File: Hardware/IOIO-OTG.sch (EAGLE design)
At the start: 53 parts, among them Q1 IRLML2244, Q2 2N7002PW, U1 PIC24FJ256GB206, U14 SWITCH_SPDT, U2 TPS6214X"", U3 VREG_MIC5216

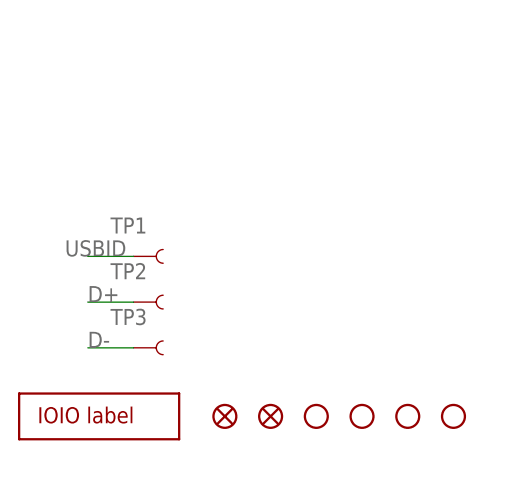
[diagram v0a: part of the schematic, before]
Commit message: More changes:
-removed test-points from below the microAB
-Moved "PWR" LED and RES out just a bit more to clear headers on the OTG
w/ Headers
-Created and added a new TRIMPOT FP per Bob's request
-Added T-Stop around the PIC to allow Tyler T. to be able to inspect the
PIC with the AOI
-Also added a new new microAB FP
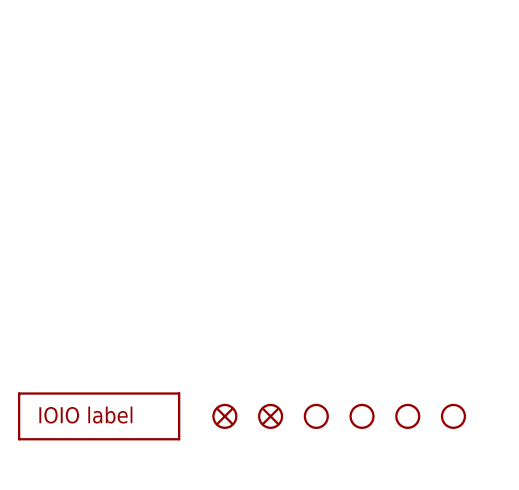
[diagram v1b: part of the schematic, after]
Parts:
- removed TP1, TP2, TP3: TEST-POINT3, SparkFun-Passives:TEST-POINT3
- R3: device SparkFun-Electromechanical:TRIMPOTTRIMPOT-5MM -> Testing:TRIMPOTSMD_STANDARD
- U4: device Testing:USB-AB"" -> Testing:USB-AB"""
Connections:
- net D+: no longer TP2.1
- net D-: no longer TP3.1
- net USBID: no longer TP1.1
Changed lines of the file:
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@@
 <part name="JP1" library="SparkFun" deviceset="M03" device="PTH" value="VIN"/>
 <part name="JP3" library="SparkFun" deviceset="M01" device="PTH"/>
-<part name="R3" library="SparkFun-Electromechanical" deviceset="TRIMPOT" device="TRIMPOT-5MM" value="TS53YL502MR10">
+<part name="R3" library="Testing" deviceset="TRIMPOT" device="SMD_STANDARD" value="TS53YL502MR10">
 <attribute name="PART#" value="TS53YL502MR10"/>
 </part>
@@
 <part name="JP8" library="SparkFun" deviceset="FIDUCIAL" device="UFIDUCIAL"/>
 <part name="JP16" library="SparkFun" deviceset="FIDUCIAL" device="UFIDUCIAL"/>
-<part name="TP1" library="SparkFun-Passives" deviceset="TEST-POINT" device="3"/>
-<part name="TP2" library="SparkFun-Passives" deviceset="TEST-POINT" device="3"/>
-<part name="TP3" library="SparkFun-Passives" deviceset="TEST-POINT" device="3"/>
 <part name="U$6" library="SparkFun-Aesthetics" deviceset="IOIO-OTG" device=""/>
-<part name="U4" library="Testing" deviceset="USB-AB" device="&quot;&quot;"/>
+<part name="U4" library="Testing" deviceset="USB-AB" device="&quot;&quot;&quot;"/>
 <part name="U2" library="SparkFun-PowerIC" deviceset="TPS6214X" device="&quot;&quot;"/>
 </parts>
@@
 <instance part="JP8" gate="G$1" x="27.94" y="10.16"/>
 <instance part="JP16" gate="G$1" x="33.02" y="10.16"/>
-<instance part="TP1" gate="G$1" x="17.78" y="27.94" smashed="yes">
-<attribute name="NAME" x="15.24" y="30.48" size="1.778" layer="95"/>
-</instance>
-<instance part="TP2" gate="G$1" x="17.78" y="22.86" smashed="yes">
-<attribute name="NAME" x="15.24" y="25.4" size="1.778" layer="95"/>
-</instance>
-<instance part="TP3" gate="G$1" x="17.78" y="17.78" smashed="yes">
-<attribute name="NAME" x="15.24" y="20.32" size="1.778" layer="95"/>
-</instance>
 <instance part="U$6" gate="G$1" x="5.08" y="7.62"/>
 <instance part="U4" gate="G$1" x="254" y="53.34" rot="MR180"/>
@@
 <pinref part="U4" gate="G$1" pin="D-"/>
 </segment>
-<segment>
-<pinref part="TP3" gate="G$1" pin="1"/>
-<wire x1="17.78" y1="17.78" x2="12.7" y2="17.78" width="0.1524" layer="91"/>
-<label x="12.7" y="17.78" size="1.778" layer="95"/>
-</segment>
 </net>
 <net name="D+" class="0">
@@
 <label x="203.2" y="53.34" size="1.778" layer="95"/>
 <pinref part="U4" gate="G$1" pin="D+"/>
-</segment>
-<segment>
-<pinref part="TP2" gate="G$1" pin="1"/>
-<wire x1="17.78" y1="22.86" x2="12.7" y2="22.86" width="0.1524" layer="91"/>
-<label x="12.7" y="22.86" size="1.778" layer="95"/>
 </segment>
 </net>
@@
 <label x="68.58" y="66.04" size="1.778" layer="95"/>
 </segment>
-<segment>
-<pinref part="TP1" gate="G$1" pin="1"/>
-<wire x1="17.78" y1="27.94" x2="12.7" y2="27.94" width="0.1524" layer="91"/>
-<label x="10.16" y="27.94" size="1.778" layer="95"/>
-</segment>
-</net>
+</net>

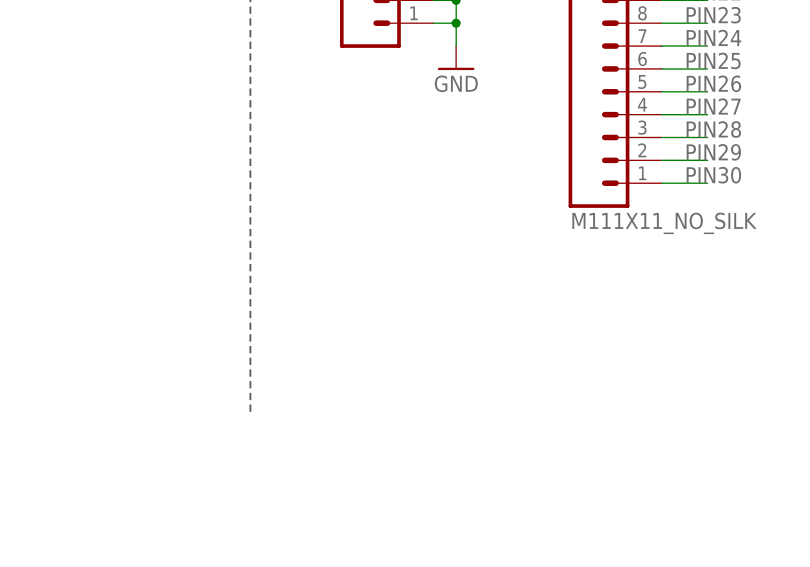
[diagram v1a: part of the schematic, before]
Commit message: Added VBUS test-point and Tstop around VREG
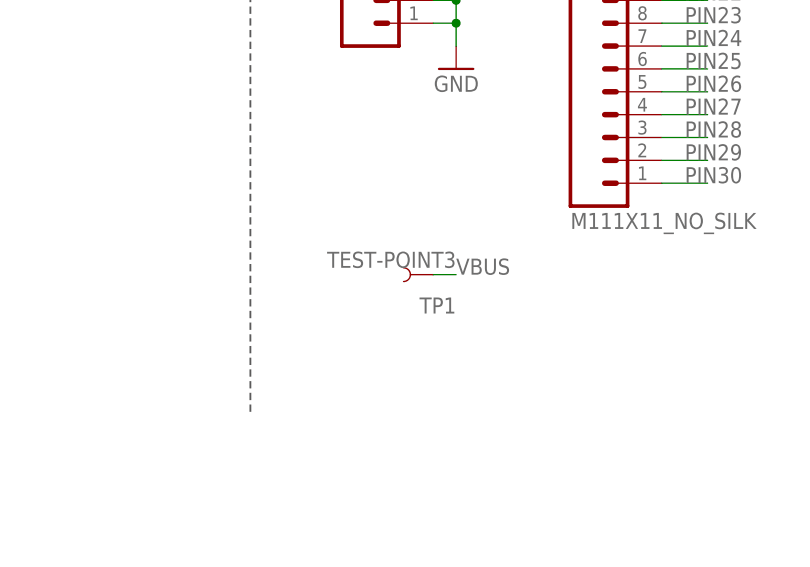
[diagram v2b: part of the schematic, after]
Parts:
- added TP1: TEST-POINT3, SparkFun-Passives:TEST-POINT3
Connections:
- net VBUS: now also TP1.1
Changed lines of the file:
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@@
 <part name="U4" library="Testing" deviceset="USB-AB" device="&quot;&quot;&quot;"/>
 <part name="U2" library="SparkFun-PowerIC" deviceset="TPS6214X" device="&quot;&quot;"/>
+<part name="TP1" library="SparkFun-Passives" deviceset="TEST-POINT" device="3"/>
 </parts>
 <sheets>
@@
 <instance part="U4" gate="G$1" x="254" y="53.34" rot="MR180"/>
 <instance part="U2" gate="G$1" x="111.76" y="228.6"/>
+<instance part="TP1" gate="G$1" x="309.88" y="38.1" rot="R180"/>
 </instances>
 <busses>
@@
 <label x="281.94" y="226.06" size="1.778" layer="95"/>
 </segment>
-</net>
+<segment>
+<pinref part="TP1" gate="G$1" pin="1"/>
+<wire x1="309.88" y1="38.1" x2="312.42" y2="38.1" width="0.1524" layer="91"/>
+<label x="312.42" y="38.1" size="1.778" layer="95"/>
+</segment>
+</net>

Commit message: Consistency fixes
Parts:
- C10: device SparkFun-Passives:CAP_POL1206 -> SparkFun-Capacitors:CAP_POL1206
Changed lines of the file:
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@@
 </part>
 <part name="R2" library="SparkFun-Resistors" deviceset="RESISTOR" device="0603-RES" value="100k"/>
-<part name="C10" library="SparkFun-Passives" deviceset="CAP_POL" device="1206" value="10uF">
+<part name="C10" library="SparkFun-Capacitors" deviceset="CAP_POL" device="1206" value="10uF">
 <attribute name="PART#" value="TAJA106K016RNJ"/>
 </part>

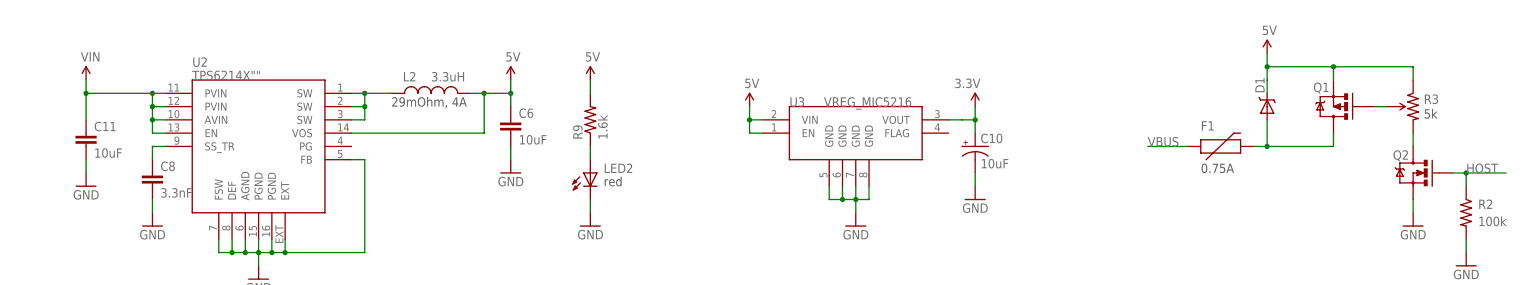
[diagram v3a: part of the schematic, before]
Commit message: Final 6.5.0 inconsistency fixes
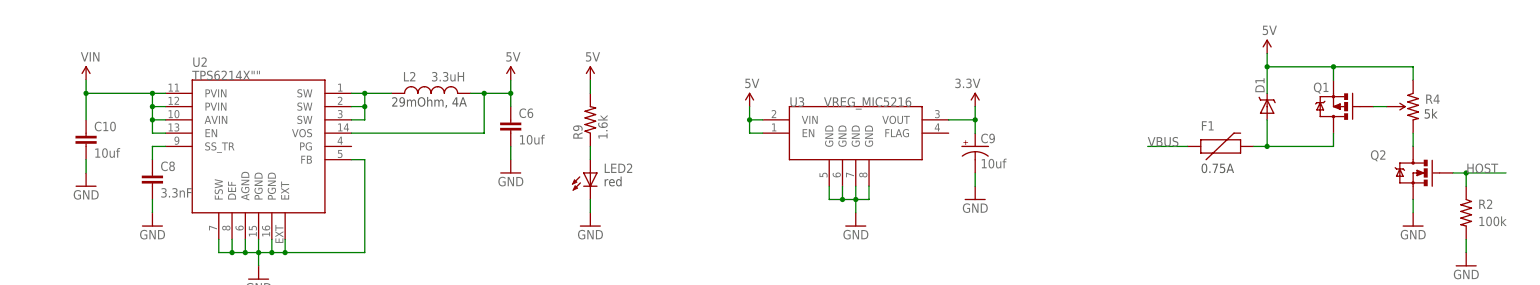
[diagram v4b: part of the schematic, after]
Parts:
- removed C11: 10uF, SparkFun-Passives:CAP1210
- added C9: 10uf, SparkFun-Capacitors:CAP_POL1206
- C10: value 10uF -> 10uf; device SparkFun-Capacitors:CAP_POL1206 -> SparkFun-Passives:CAP1210; PART# TAJA106K016RNJ -> (none)
- C6: value 10uF -> 10uf; PART# LMK212BJ106KG-T -> (none)
- D1: value B340A -> DIODE-SCHOTTKY_; PART# B340A -> (none)
- F1: PART# 0ZCA0075FF2G -> (none)
- Q2: value 2N7002PW -> MOSFET-NCHANNEL2N7002PW"; device SparkFun-DiscreteSemi:MOSFET-NCHANNELSOT323 -> SparkFun-DiscreteSemi:MOSFET-NCHANNEL2N7002PW"; PART# 2N7002PW -> (none)
- R4: value TS53YL502MR10 -> TRIMPOTSMD_STANDARD; PART# TS53YL502MR10 -> (none)
- renumbered R3 to R4
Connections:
- net 3.3V: now also C9.+; no longer C10.+
- net GND: now also C10.2, C9.-; no longer C10.-, C11.2
- net VIN: now also C10.1; no longer C11.1

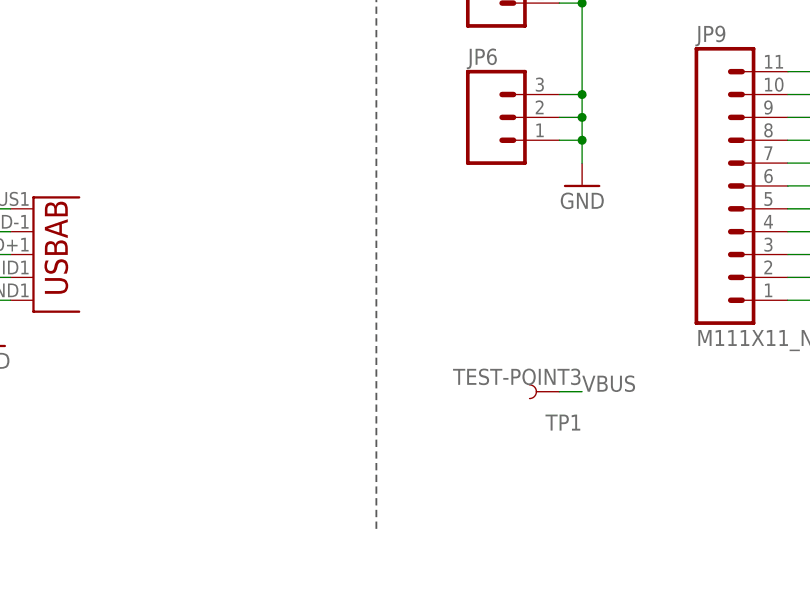
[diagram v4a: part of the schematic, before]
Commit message: Added test-points
3 new test-points:
D+
D-
USBID
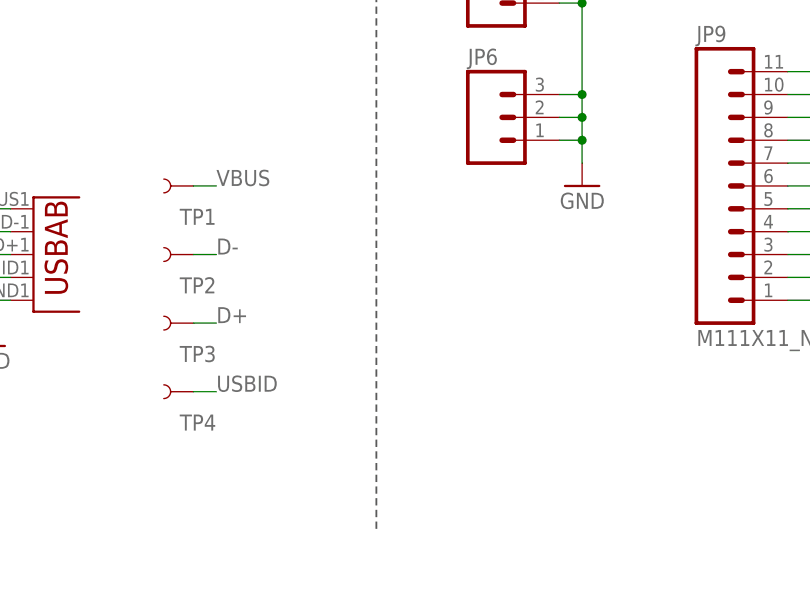
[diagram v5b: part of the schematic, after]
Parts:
- added TP2, TP3, TP4: TEST-POINT3, SparkFun-Passives:TEST-POINT3
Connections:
- net D+: now also TP3.1
- net D-: now also TP2.1
- net USBID: now also TP4.1
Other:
- moved on the sheet: TP1
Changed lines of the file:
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@@
 <part name="Q2" library="SparkFun-DiscreteSemi" deviceset="MOSFET-NCHANNEL" device="2N7002PW&quot;"/>
 <part name="R4" library="Testing" deviceset="TRIMPOT" device="SMD_STANDARD"/>
+<part name="TP2" library="SparkFun-Passives" deviceset="TEST-POINT" device="3"/>
+<part name="TP3" library="SparkFun-Passives" deviceset="TEST-POINT" device="3"/>
+<part name="TP4" library="SparkFun-Passives" deviceset="TEST-POINT" device="3"/>
 </parts>
 <sheets>
@@
 <instance part="U4" gate="G$1" x="254" y="53.34" rot="MR180"/>
 <instance part="U2" gate="G$1" x="111.76" y="228.6"/>
-<instance part="TP1" gate="G$1" x="309.88" y="38.1" rot="R180"/>
+<instance part="TP1" gate="G$1" x="269.24" y="60.96" smashed="yes" rot="R180">
+<attribute name="NAME" x="271.78" y="58.42" size="1.778" layer="95" rot="R180"/>
+</instance>
 <instance part="C9" gate="G$1" x="248.92" y="226.06"/>
 <instance part="C10" gate="G$1" x="78.74" y="226.06"/>
@@
 <instance part="R4" gate="R?" x="332.74" y="233.68" smashed="yes" rot="MR270">
 <attribute name="NAME" x="335.026" y="235.9914" size="1.778" layer="95" rot="MR180"/>
+</instance>
+<instance part="TP2" gate="G$1" x="269.24" y="53.34" smashed="yes" rot="R180">
+<attribute name="NAME" x="271.78" y="50.8" size="1.778" layer="95" rot="R180"/>
+</instance>
+<instance part="TP3" gate="G$1" x="269.24" y="45.72" smashed="yes" rot="R180">
+<attribute name="NAME" x="271.78" y="43.18" size="1.778" layer="95" rot="R180"/>
+</instance>
+<instance part="TP4" gate="G$1" x="269.24" y="38.1" smashed="yes" rot="R180">
+<attribute name="NAME" x="271.78" y="35.56" size="1.778" layer="95" rot="R180"/>
 </instance>
 </instances>
@@
 <pinref part="U4" gate="G$1" pin="D-"/>
 </segment>
+<segment>
+<pinref part="TP2" gate="G$1" pin="1"/>
+<wire x1="269.24" y1="53.34" x2="271.78" y2="53.34" width="0.1524" layer="91"/>
+<label x="271.78" y="53.34" size="1.778" layer="95"/>
+</segment>
 </net>
 <net name="D+" class="0">
@@
 <label x="203.2" y="53.34" size="1.778" layer="95"/>
 <pinref part="U4" gate="G$1" pin="D+"/>
+</segment>
+<segment>
+<pinref part="TP3" gate="G$1" pin="1"/>
+<wire x1="269.24" y1="45.72" x2="271.78" y2="45.72" width="0.1524" layer="91"/>
+<label x="271.78" y="45.72" size="1.778" layer="95"/>
 </segment>
 </net>
@@
 <label x="68.58" y="66.04" size="1.778" layer="95"/>
 </segment>
+<segment>
+<pinref part="TP4" gate="G$1" pin="1"/>
+<wire x1="269.24" y1="38.1" x2="271.78" y2="38.1" width="0.1524" layer="91"/>
+<label x="271.78" y="38.1" size="1.778" layer="95"/>
+</segment>
 </net>
 <net name="VBUS" class="0">
@@
 <segment>
 <pinref part="TP1" gate="G$1" pin="1"/>
-<wire x1="309.88" y1="38.1" x2="312.42" y2="38.1" width="0.1524" layer="91"/>
-<label x="312.42" y="38.1" size="1.778" layer="95"/>
-</segment>
-</net>
+<wire x1="269.24" y1="60.96" x2="271.78" y2="60.96" width="0.1524" layer="91"/>
+<label x="271.78" y="60.96" size="1.778" layer="95"/>
+</segment>
+</net>

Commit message: Adding in hardware changes from Pete
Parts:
- removed LED1: LY L29K-J1K2-26-Z, SparkFun-LED:LED0603
- removed LED2: LS L29K-G1J2-1-Z, SparkFun:LED0603
- removed TP4: TEST-POINT3, SparkFun-Passives:TEST-POINT3
- removed U$1: CREATIVE_COMMONS, SparkFun-Aesthetics:CREATIVE_COMMONS
- removed U$2: M191X19_NO_SILK, SparkFun-Connectors:M191X19_NO_SILK
- removed U14: SWITCH_SPDT, SparkFun-Electromechanical:SWITCH_SPDT
- removed U4: (no value), Testing:USB-AB"""
- added C11: 10uF, SparkFun-Capacitors:10UF50V20%(1210)
- added D2: DZ2J160M0L, SparkFun-DiscreteSemi:DIODE-ZENERDZ2J150M0L
- added D3: Yellow, SparkFun-LED:LED-YELLOW0603-SMART
- added D5: Red, SparkFun-LED:LED-RED0603-SMART
- added FRAME2: FRAME-LEDGER, SparkFun-Aesthetics:FRAME-LEDGER
- added JP20: M191X19_NO_SILK, SparkFun-Connectors:M191X19_NO_SILK
- added JP21: AB MICRO USB, SparkFun-Connectors:USB-ABCONN-11794
- added LOGO1: OSHW-LOGOS, SparkFun-Aesthetics:OSHW-LOGOS
- added LOGO2: SFE_LOGO_NAME_FLAME.1_INCH, SparkFun-Aesthetics:SFE_LOGO_NAME_FLAME.1_INCH
- added LOGO3: SFE_LOGO_FLAME.1_INCH, SparkFun-Aesthetics:SFE_LOGO_FLAME.1_INCH
- added Q3: MOSFET-NCHANNELAO3404A, SparkFun-DiscreteSemi:MOSFET-NCHANNELAO3404A
- added R3: TS53YL502MR10, SparkFun-Electromechanical:TRIMPOTRES-11156
- added S1: SWITCH_SPDT, SparkFun-Electromechanical:SWITCH_SPDT
- C1, C2, C3, C4, C5: device SparkFun-Capacitors:CAP0603-CAP -> SparkFun-Capacitors:0.1UF-25V(+80/-20%)(0603)
- C10: value 10uf -> 10uF; device SparkFun-Passives:CAP1210 -> SparkFun-Capacitors:10UF-16V-10%(TANT); PART# (none) -> TAJA106K016RNJ
- C6: value 10uf -> 10uF; device SparkFun-Passives:CAP0805 -> SparkFun-Capacitors:10UF10V10%(0805); PART# (none) -> LMK212BJ106KG-T
- C7: device SparkFun:CAP_POL1206 -> SparkFun-Capacitors:10UF-16V-10%(TANT)
- C8: device SparkFun-Capacitors:CAP0603-CAP -> SparkFun-Capacitors:3.3NF-100V-10%(0603)
- C9: value 10uf -> 0.1uF; device SparkFun-Capacitors:CAP_POL1206 -> SparkFun-Capacitors:0.1UF-25V(+80/-20%)(0603)
- D1: value DIODE-SCHOTTKY_ -> B340A; device SparkFun-DiscreteSemi:DIODE-SCHOTTKY_ -> SparkFun-DiscreteSemi:DIODE-SCHOTTKY-B340A; PART# (none) -> B340A
- F1: value PTCSMD -> 0.75A; PART# (none) -> 0ZCA0075FF2G
- JP1: value VIN -> (none)
- JP19: value JST Connector -> JST; device SparkFun:M02-JST-2MM-SMT -> SparkFun-Connectors:JST_2MM_MALE
- JP4: value 5V -> (none)
- L1: device SparkFun-Passives:INDUCTOR0603 -> SparkFun-Passives:INDUCTOR30OHM,1.8A
- L2: device SparkFun-Passives:INDUCTORCR54 -> SparkFun-Passives:INDUCTORCR54-3.3UH
- Q1: device SparkFun-DiscreteSemi:MOSFET-PCHANNELSMD -> SparkFun-DiscreteSemi:MOSFET-PCHANNELIRLML2244
- Q2: value MOSFET-NCHANNEL2N7002PW" -> 2N7002PW; device SparkFun-DiscreteSemi:MOSFET-NCHANNEL2N7002PW" -> SparkFun-DiscreteSemi:MOSFET-NCHANNEL2N7002PW; PART# (none) -> 2N7002PW
- R1: value 10k -> 10K; device SparkFun-Resistors:RESISTOR0603-RES -> SparkFun-Resistors:10KOHM-1/10W-1%(0603)0603
- R2: device SparkFun-Resistors:RESISTOR0603-RES -> SparkFun-Resistors:100KOHM-1/10W-1%(0603)
- R4: value TRIMPOTSMD_STANDARD -> 3.3k; device Testing:TRIMPOTSMD_STANDARD -> SparkFun-Resistors:3.3KOHM1/10W1%(0603)
- R7: device SparkFun-Resistors:RESISTOR0603-RES -> SparkFun-Resistors:750OHM1/10W1%(0603)0603
- R8: device SparkFun-Resistors:RESISTOR0603-RES -> SparkFun-Resistors:470OHM1/10W1%(0603)
- R9: value 1.6k -> 1.6K; device SparkFun-Resistors:RESISTOR0603-RES -> SparkFun-Resistors:1.6KOHM-1/10W-1%(0603)0603
- U1: device SparkFun-DigitalIC:PIC24FXXXDAX06 -> SparkFun-DigitalIC:PIC24FXXXGPX06
- U2: value TPS6214X"" -> TPS62133RGTT; device SparkFun-PowerIC:TPS6214X"" -> SparkFun-PowerIC:TPS62133RGTT""
- U3: value VREG_MIC5216 -> MIC5216; device SparkFun-PowerIC:VREG_MIC5216 -> SparkFun-PowerIC:V_REG_MIC5216
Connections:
- new net ANCHOR1: JP21.SHIELD
- new net N$12: D2.A, Q3.G, R4.1
- net 3.3V: now also C10.+; no longer C9.+
- net 5V: now also R3.CCW; no longer R4.CCW
- net BOOT: now also D3.C; no longer LED1.C
- net D+: now also JP21.D+, TP2.1; no longer TP3.1, U4.D+
- net D-: now also JP21.D-, TP3.1; no longer TP2.1, U4.D-
- net GND: now also C10.-, C11.2, C9.2, D5.C, JP19.-, JP21.GND, Q3.S, R4.2, S1.S; no longer C10.2, C9.-, JP19.1, LED2.C, U14.O, U4.GND
- net N$1: now also R3.WIPER; no longer R4.WIPER
- net N$2: now also D3.A; no longer LED1.A
- net N$3: now also D5.A; no longer LED2.A
- net N$8: now also R3.CW; no longer R4.CW
- net PIN1: now also JP20.1; no longer U$2.1
- net PIN10: now also JP20.10; no longer U$2.10
- net PIN11: now also JP20.11; no longer U$2.11
- net PIN12: now also JP20.12; no longer U$2.12
- net PIN13: now also JP20.13; no longer U$2.13
- net PIN14: now also JP20.14; no longer U$2.14
- net PIN15: now also JP20.15; no longer U$2.15
- net PIN16: now also JP20.16; no longer U$2.16
- net PIN17: now also JP20.17; no longer U$2.17
- net PIN18: now also JP20.18; no longer U$2.18
- net PIN19: now also JP20.19; no longer U$2.19
- net PIN2: now also JP20.2; no longer U$2.2
- net PIN3: now also JP20.3; no longer U$2.3
- net PIN4: now also JP20.4; no longer U$2.4
- net PIN5: now also JP20.5; no longer U$2.5
- net PIN6: now also JP20.6; no longer U$2.6
- net PIN7: now also JP20.7; no longer U$2.7
- net PIN8: now also JP20.8; no longer U$2.8
- net PIN9: now also JP20.9; no longer U$2.9
- net USBID: now also JP21.USBID, S1.P, TP1.1; no longer TP4.1, U14.P, U4.USBID
- net VBUS: now also JP21.VBUS; no longer TP1.1, U4.VBUS
- net VIN: now also C11.1, C9.1, D2.C, JP19.+, Q3.D; no longer C10.1, JP19.2
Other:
- note added: "V22b"
- note added: "revised by A.Weiss, Pete Lewis"
- note removed: "revised by A.Weiss"
- moved on the sheet: C1, C2, C3, C4, C5, C6, C7, C8, F1, JP1, JP14, JP15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

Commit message: Value text object to sch for D1, D2, Q1, Q2, Q3
I used part #s for values (rather than the "values") for these
components. This is to ensure production (and users) will know when they
are a different component, when looking at the schematic. Note they are
text objects living in the wild, and not actually part of the device in
the library. Although, the values are inside the properties for each
device as well.
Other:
- note added: "2N7002PW"
- note added: "AO3404A"
- note added: "B340A"
- note added: "DZ2J160M0L"
- note added: "IRLML2244"
- moved on the sheet: D1, D2, F1, JP19, Q2, Q3, R2, R3, R4
